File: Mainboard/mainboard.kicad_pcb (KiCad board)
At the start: 2 copper layers, 66 x 30 mm, 85 parts, among them J1 Conn_01x04_Pin, Q1 Q_PMOS_GSD, Q2 Q_PMOS_GSD, U1 AP2205-3.0, U2 BQ21080, U3 LIS2DW12, U4 STM32L412KBTx, U5 BH1730, Y1 32.768k

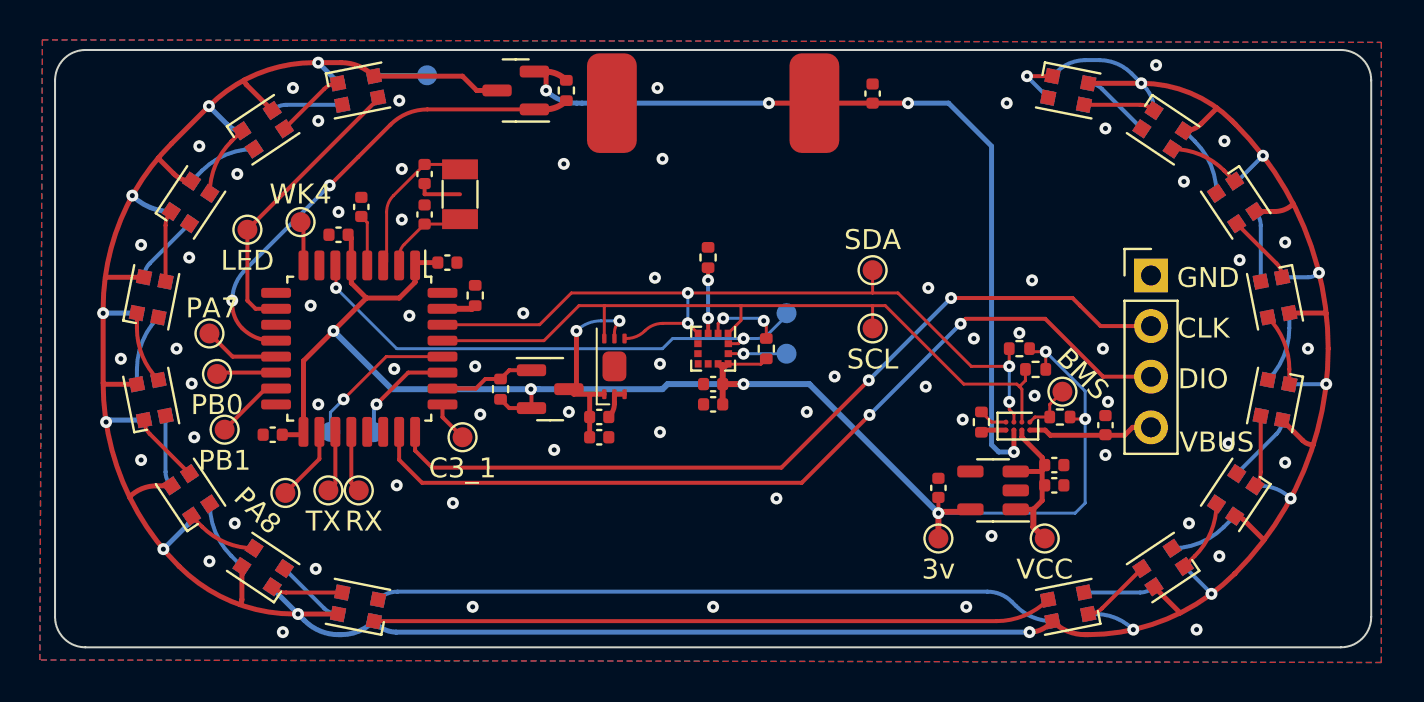
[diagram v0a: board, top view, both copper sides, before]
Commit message: New hardware; attempt to correct BMS failures, better layout and routing, bom only change to allow swap to USB DFU Bootloader/upload
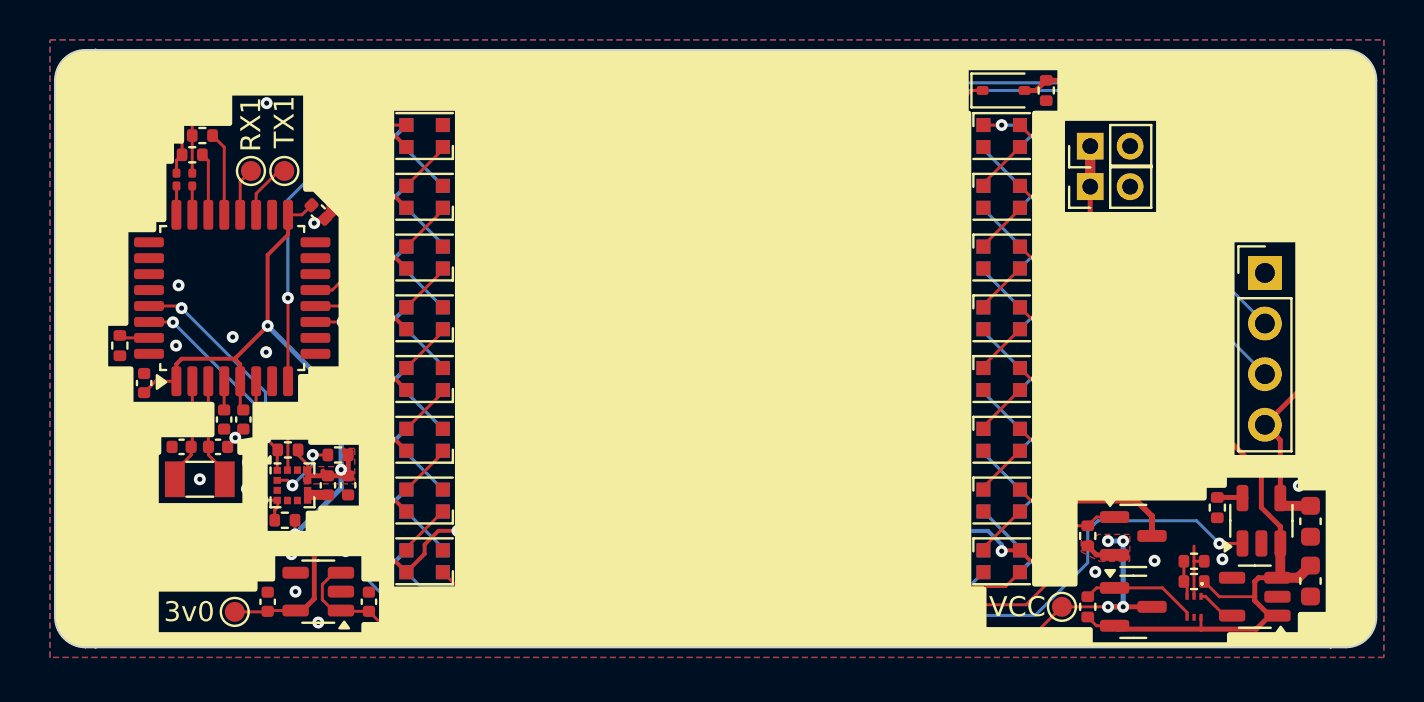
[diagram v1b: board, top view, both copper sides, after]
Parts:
- removed BT1: 200mAh, Components:battery_20x30
- removed C1: 10u, Capacitor_SMD:C_0402_1005Metric
- removed C11, C2: 1u, Capacitor_SMD:C_0402_1005Metric
- removed REF** (x2), REF**1 (x2), REF**10 (x2), REF**11 (x2), REF**12 (x2), REF**13 (x2), REF**14 (x2), REF**15 (x2), REF**2 (x2), REF**3 (x2), REF**4 (x2), REF**5 (x2), REF**6 (x2), REF**7 (x2), REF**8 (x2), REF**9 (x2): LED_WS2812B-2020_PLCC4_2.0x2.0mm, LED_SMD:LED_WS2812B-2020_PLCC4_2.0x2.0mm
- removed REF**: TestPoint_Pad_D1.0mm, TestPoint:TestPoint_Pad_D1.0mm
- removed TP1: PB0, TestPoint:TestPoint_Pad_D1.0mm
- removed TP10: 3v, TestPoint:TestPoint_Pad_D1.0mm
- removed TP11: BMS, TestPoint:TestPoint_Pad_D1.0mm
- removed TP12: LED, TestPoint:TestPoint_Pad_D1.0mm
- removed TP13: WK4, TestPoint:TestPoint_Pad_D1.0mm
- removed TP14: C2_1, TestPoint:TestPoint_Pad_D1.0mm
- removed TP15: C2_2, TestPoint:TestPoint_Pad_D1.0mm
- removed TP16: C3_1, TestPoint:TestPoint_Pad_D1.0mm
- removed TP17: TX, TestPoint:TestPoint_Pad_D1.0mm
- removed TP2: PA7, TestPoint:TestPoint_Pad_D1.0mm
- removed TP3: PB1, TestPoint:TestPoint_Pad_D1.0mm
- removed TP4: PA8, TestPoint:TestPoint_Pad_D1.0mm
- removed TP5: SDA, TestPoint:TestPoint_Pad_D1.0mm
- removed TP6: SCL, TestPoint:TestPoint_Pad_D1.0mm
- removed TP7: INT1, TestPoint:TestPoint_Pad_D1.0mm
- removed TP8: INT2, TestPoint:TestPoint_Pad_D1.0mm
- added 3v0: 3v, TestPoint:TestPoint_Pad_D1.0mm, F.Cu at (161.7, 104.4)
- added D1: WS2812B-2020, LED_SMD:LED_WS2812B-2020_PLCC4_2.0x2.0mm, F.Cu at (171.2, 80.5)
- added D10: WS2812B-2020, LED_SMD:LED_WS2812B-2020_PLCC4_2.0x2.0mm, F.Cu at (200.2, 98.8)
- added D11: WS2812B-2020, LED_SMD:LED_WS2812B-2020_PLCC4_2.0x2.0mm, F.Cu at (200.2, 95.8)
- added D12: WS2812B-2020, LED_SMD:LED_WS2812B-2020_PLCC4_2.0x2.0mm, F.Cu at (200.2, 92.7)
- added D13: WS2812B-2020, LED_SMD:LED_WS2812B-2020_PLCC4_2.0x2.0mm, F.Cu at (200.2, 89.7)
- added D14: WS2812B-2020, LED_SMD:LED_WS2812B-2020_PLCC4_2.0x2.0mm, F.Cu at (200.2, 86.6)
- added D15: WS2812B-2020, LED_SMD:LED_WS2812B-2020_PLCC4_2.0x2.0mm, F.Cu at (200.2, 83.6)
- added D16: WS2812B-2020, LED_SMD:LED_WS2812B-2020_PLCC4_2.0x2.0mm, F.Cu at (200.2, 80.5)
- added D17: WS2812B-2020, LED_SMD:LED_WS2812B-2020_PLCC4_2.0x2.0mm, B.Cu at (200.2, 80.5)
- added D18: WS2812B-2020, LED_SMD:LED_WS2812B-2020_PLCC4_2.0x2.0mm, B.Cu at (200.2, 83.6)
- added D19: WS2812B-2020, LED_SMD:LED_WS2812B-2020_PLCC4_2.0x2.0mm, B.Cu at (200.2, 86.6)
- added D2: WS2812B-2020, LED_SMD:LED_WS2812B-2020_PLCC4_2.0x2.0mm, F.Cu at (171.2, 83.6)
- added D20: WS2812B-2020, LED_SMD:LED_WS2812B-2020_PLCC4_2.0x2.0mm, B.Cu at (200.2, 89.7)
- added D21: WS2812B-2020, LED_SMD:LED_WS2812B-2020_PLCC4_2.0x2.0mm, B.Cu at (200.2, 92.7)
- added D22: WS2812B-2020, LED_SMD:LED_WS2812B-2020_PLCC4_2.0x2.0mm, B.Cu at (200.2, 95.8)
- added D23: WS2812B-2020, LED_SMD:LED_WS2812B-2020_PLCC4_2.0x2.0mm, B.Cu at (200.2, 98.8)
- added D24: WS2812B-2020, LED_SMD:LED_WS2812B-2020_PLCC4_2.0x2.0mm, B.Cu at (200.2, 101.9)
- added D25: WS2812B-2020, LED_SMD:LED_WS2812B-2020_PLCC4_2.0x2.0mm, B.Cu at (171.2, 101.9)
- added D26: WS2812B-2020, LED_SMD:LED_WS2812B-2020_PLCC4_2.0x2.0mm, B.Cu at (171.2, 98.8)
- added D27: WS2812B-2020, LED_SMD:LED_WS2812B-2020_PLCC4_2.0x2.0mm, B.Cu at (171.2, 95.8)
- added D28: WS2812B-2020, LED_SMD:LED_WS2812B-2020_PLCC4_2.0x2.0mm, B.Cu at (171.2, 92.7)
- added D29: WS2812B-2020, LED_SMD:LED_WS2812B-2020_PLCC4_2.0x2.0mm, B.Cu at (171.2, 89.7)
- added D3: WS2812B-2020, LED_SMD:LED_WS2812B-2020_PLCC4_2.0x2.0mm, F.Cu at (171.2, 86.6)
- added D30: WS2812B-2020, LED_SMD:LED_WS2812B-2020_PLCC4_2.0x2.0mm, B.Cu at (171.2, 86.6)
- added D31: WS2812B-2020, LED_SMD:LED_WS2812B-2020_PLCC4_2.0x2.0mm, B.Cu at (171.2, 83.6)
- added D32: WS2812B-2020, LED_SMD:LED_WS2812B-2020_PLCC4_2.0x2.0mm, B.Cu at (171.2, 80.5)
- added D33: D, Diode_SMD:D_SOD-323, F.Cu at (200.2, 78.2)
- added D4: WS2812B-2020, LED_SMD:LED_WS2812B-2020_PLCC4_2.0x2.0mm, F.Cu at (171.2, 89.7)
- added D5: WS2812B-2020, LED_SMD:LED_WS2812B-2020_PLCC4_2.0x2.0mm, F.Cu at (171.2, 92.7)
- added D6: WS2812B-2020, LED_SMD:LED_WS2812B-2020_PLCC4_2.0x2.0mm, F.Cu at (171.2, 95.8)
- added D7: WS2812B-2020, LED_SMD:LED_WS2812B-2020_PLCC4_2.0x2.0mm, F.Cu at (171.2, 98.8)
- added D8: WS2812B-2020, LED_SMD:LED_WS2812B-2020_PLCC4_2.0x2.0mm, F.Cu at (171.2, 101.9)
- added D9: WS2812B-2020, LED_SMD:LED_WS2812B-2020_PLCC4_2.0x2.0mm, F.Cu at (200.2, 101.9)
- added IC1: TLV3691IDPFR, Components:TLV3691IDPFR, F.Cu at (209.8, 104.1)
- added J2: Conn_01x02_Socket, Connector_PinHeader_2.00mm:PinHeader_1x02_P2.00mm_Vertical, F.Cu at (204.6, 83.1)
- added J3: Conn_01x02_Socket, Connector_PinHeader_2.00mm:PinHeader_1x02_P2.00mm_Vertical, F.Cu at (204.6, 81.0)
- added R10: 100k, Resistor_SMD:R_0402_1005Metric, F.Cu at (202.4, 78.2)
- added R11: 2M, Resistor_SMD:R_0402_1005Metric, F.Cu at (209.8, 101.9)
- added R12: R_Small, Resistor_SMD:R_0201_0603Metric, F.Cu at (158.8, 82.7)
- added R13: R_Small, Resistor_SMD:R_0402_1005Metric, F.Cu at (159.5, 81.5)
- added R14: R_Small, Resistor_SMD:R_0402_1005Metric, F.Cu at (160.0, 80.5)
- added TX1: TX, TestPoint:TestPoint_Pad_D1.0mm, F.Cu at (164.2, 82.3)
- C14, C15: value 100n -> 10u; footprint Capacitor_SMD:C_0402_1005Metric -> Capacitor_SMD:C_0603_1608Metric
- R1: value 10k -> 10M
- R3: value 0 -> R_Small; footprint Resistor_SMD:R_0402_1005Metric -> Resistor_SMD:R_0201_0603Metric
- R4: value 10k -> 100k
- R5: value 10k -> 1M8
- R8: value 100k -> 10k
- U2: value BQ21080 -> TPS7A0218PDBVR; footprint Components:Texas_DSBGA-8-1.04x1.59mm -> Package_TO_SOT_SMD:SOT-23-5
- U5: value BH1730 -> MCP73832-2-OT; footprint Components:WSOF6 -> Package_TO_SOT_SMD:SOT-23-5
- moved Q2 38.2 mm to (206.8, 100.6), turned to 0 degrees
- moved R7 37.8 mm to (164.2, 99.8)
- moved R6 37.7 mm to (164.3, 96.3)
- moved R8 36.5 mm to (211.0, 99.2)
- moved C15 36.4 mm to (215.6, 102.8), turned to -90 degrees
- moved C14 36.1 mm to (215.6, 99.8), turned to -90 degrees
- moved C8 34.9 mm to (168.4, 103.9), turned to 90 degrees
- moved R9 34.4 mm to (204.5, 100.6), turned to 90 degrees
- moved U1 34.2 mm to (165.9, 103.4)
- moved C9 34.1 mm to (163.3, 103.9)
- moved U5 33.4 mm to (213.2, 99.8)
- moved Q1 31.2 mm to (206.8, 104.1)
- moved R3 26.2 mm to (159.5, 82.7), turned to 90 degrees
- moved U3 22.2 mm to (164.6, 98.0), turned to 0 degrees
- moved R2 22.1 mm to (166.9, 96.5), turned to 180 degrees
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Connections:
- net Net-(U4-PH3) renamed /boot
- C14 pad 1: ALVCC -> VBUS
- C15 pad 1: ALVCC -> +BATT
- Q1 pad 1: BH1730PowerCtrl -> Net-(IC1-OUT)
- Q1 pad 2: +3V0 -> +BATT
- Q1 pad 3: ALVCC -> VCC
- Q2 pad 2: +BATT -> VCC
- Q2 pad 3: /LED_PWR -> /LEDs/LED_PWR
- R1 pad 1: ~{BMS_INT} -> +BATT
- R1 pad 2: +3V0 -> Net-(IC1-OUT)
- R3 pad 1: GND -> Net-(U4-PA13)
- R3 pad 2: Net-(U3-SA0/SDO) -> SWDIO
- R5 pad 1: GND -> +BATT
- R5 pad 2: TS|MR -> Net-(IC1-IN-)
- R8 pad 1: +3V0 -> GND
- R8 pad 2: BH1730PowerCtrl -> Net-(U5-PROG)
- R9 pad 1: +BATT -> VCC
- U3 pad 3: Net-(U3-SA0/SDO) -> unconnected-(U3-SA0/SDO-Pad3)
- U4 pad 10: LED IN -> unconnected-(U4-PA4-Pad10)
- U4 pad 11: unconnected-(U4-PA5-Pad11) -> BMS_Stat
- U4 pad 13: Net-(U4-PA7) -> LED
- U4 pad 14: Net-(U4-PB0) -> unconnected-(U4-PB0-Pad14)
- U4 pad 15: Net-(U4-PB1) -> unconnected-(U4-PB1-Pad15)
- U4 pad 18: Net-(U4-PA8) -> unconnected-(U4-PA8-Pad18)
- U4 pad 21: unconnected-(U4-PA11-Pad21) -> USB_D-
- U4 pad 22: unconnected-(U4-PA12-Pad22) -> USB_D+
- U4 pad 23: SWDIO -> Net-(U4-PA13)
- U4 pad 24: SWCLK -> Net-(U4-PA14)
- U4 pad 25: TSC_G3_IO1 -> unconnected-(U4-PA15-Pad25)
- U4 pad 26: BH1730PowerCtrl -> unconnected-(U4-PB3-Pad26)
- U4 pad 27: TSC_G2_IO1 -> unconnected-(U4-PB4-Pad27)
- U4 pad 28: TSC_G2_IO2 -> unconnected-(U4-PB5-Pad28)
- U4 pad 8: WKUP4 -> /WKUP4
- U5 pad 1: ALVCC -> BMS_Stat
- U5 pad 3: GND -> +BATT
- U5 pad 4: SDA -> VBUS
- U5 pad 5: ALVCC -> Net-(U5-PROG)
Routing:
- net /LED_PWR: track 187.1 -> 0.00 mm, vias 15 -> 0
- net (no net): track 174.9 -> 0.00 mm, vias 1 -> 0
- net /LEDs/LED_PWR: track 0.00 -> 114.8 mm, vias 0 -> 18
- net BMS_Stat: track 0.00 -> 62.8 mm, vias 0 -> 2
- net /WKUP4: track 0.00 -> 46.2 mm, vias 0 -> 2
- net VCC: track 8.52 -> 51.0 mm, vias 0 -> 4
- net +3V0: track 83.6 -> 44.3 mm, vias 6 -> 3
- net LEDPowerCtrl: track 24.5 -> 56.1 mm, vias 2 -> 0
- net VBUS: track 6.35 -> 37.9 mm
- net Net-(D8-DOUT): track 0.00 -> 29.6 mm
- net Net-(D24-DOUT): track 0.00 -> 29.6 mm
- net SDA: track 41.1 -> 13.8 mm, vias 4 -> 2
- net SCL: track 38.6 -> 11.8 mm, vias 0 -> 2
- net SWCLK: track 42.3 -> 67.4 mm, vias 2 -> 1
- net SWDIO: track 44.2 -> 68.5 mm, vias 2 -> 1
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- added copper zone on F.Cu, net +3V0
- added copper zone on F.Cu, net VCC
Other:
- board size 66 x 30 mm -> 66.3 x 30 mm
- board text removed: "CLK"
- board text removed: "DIO"
- board text removed: "GND"
- board text removed: "VBUS"

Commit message: V2 mainboard, some firmware stuffs, free design files I guess
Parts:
- removed IC1: TLV3691IDPFR, Components:TLV3691IDPFR
- removed Q1: Q_PMOS_GSD, Package_TO_SOT_SMD:SOT-23
- removed R1: 10M, Resistor_SMD:R_0402_1005Metric
- removed R11: 2M, Resistor_SMD:R_0402_1005Metric
- removed R5: 1M8, Resistor_SMD:R_0402_1005Metric
- removed U2: TPS7A0218PDBVR, Package_TO_SOT_SMD:SOT-23-5
- added D34: D, Diode_SMD:D_SOD-323, F.Cu at (205.2, 104.0)
- added Q3: Q_PMOS_GSD, Package_TO_SOT_SMD:SOT-23, F.Cu at (208.2, 104.0)
- added R15: 100k, Resistor_SMD:R_0402_1005Metric, F.Cu at (209.3, 101.2)
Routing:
- net VBUS: track 37.9 -> 52.6 mm, vias 0 -> 1
- net +BATT: track 46.7 -> 34.4 mm
- net Net-(IC1-OUT): track 5.92 -> 0.00 mm
- net GND: track 4.98 -> 1.95 mm, vias 60 -> 65
- net Net-(IC1-IN+): track 1.96 -> 0.00 mm
- net Net-(IC1-IN-): track 1.83 -> 0.00 mm
- net VCC: track 51.0 -> 50.6 mm, vias 4 -> 0
